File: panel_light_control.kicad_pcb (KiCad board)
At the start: 4 copper layers, 90 x 100 mm, 132 parts, among them J1 Conn_01x02, J11 RJ45_Shielded, J13 HR911105A, J2 RJ45_Shielded, J6 Conn_01x04, Q1 IRF540N, Q2 IRF540N, Q3 IRF540N, U1 L7805, U2 LM324, U3 STM32F207VGT6, U4 MCP2562-E-P, U5 LAN8720A, Y1 Crystal_GND24

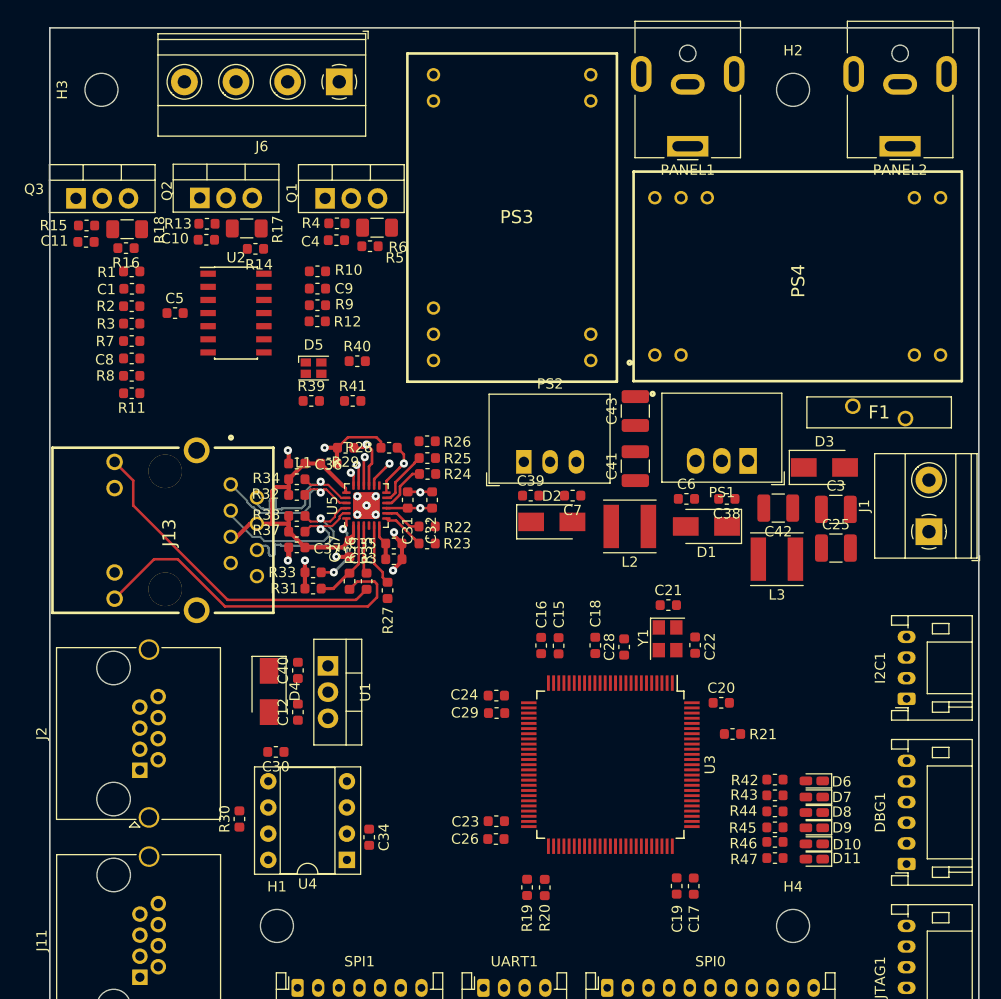
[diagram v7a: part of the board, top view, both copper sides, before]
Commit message: THT pad restring sizes increase for mechanical stability; generalized LED arrangement for more flexibility (8 bit display, CAN LED, PWM and general purpose RGB) and development-style look and feel; protection diode footprint is now THT to reduce reworking hassle should it short out due to misuse
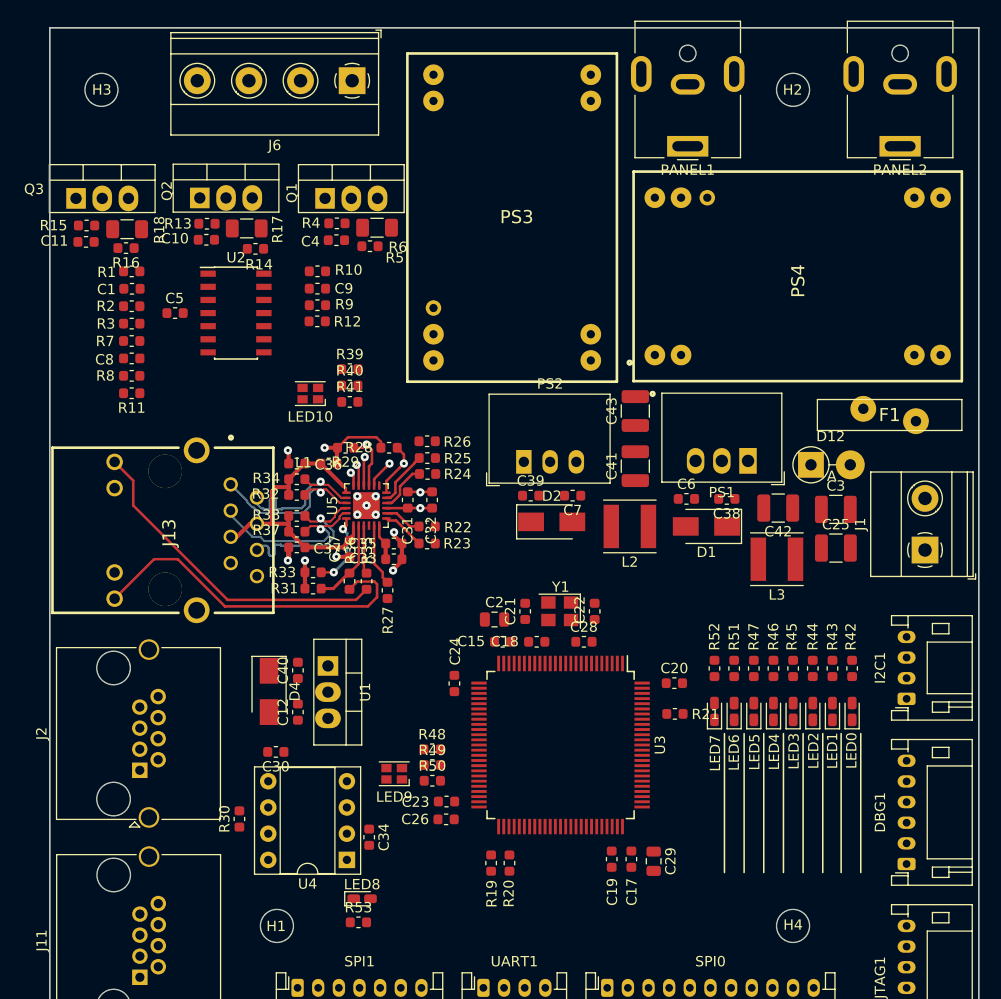
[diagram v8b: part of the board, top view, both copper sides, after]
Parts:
- removed C16: 100nF, Capacitor_SMD:C_0603_1608Metric
- removed D10: LED_WarmWhite, LED_SMD:LED_0603_1608Metric_Castellated
- removed D11: LED_ColdWhite, LED_SMD:LED_0603_1608Metric_Castellated
- removed D3: 1D4004, Diode_SMD:D_SMA
- removed D7: LED_R, LED_SMD:LED_0603_1608Metric_Castellated
- removed D8: LED_G, LED_SMD:LED_0603_1608Metric_Castellated
- removed D9: LED_B, LED_SMD:LED_0603_1608Metric_Castellated
- added C2: 4.7uF, Capacitor_SMD:C_0805_2012Metric, F.Cu at (143.1, 107.3)
- added D12: 1N4001, Diode_THT:D_DO-41_SOD81_P3.81mm_Vertical_AnodeUp, F.Cu at (173.7, 92.3)
- added LED1: LED_GN, LED_SMD:LED_0603_1608Metric_Castellated, F.Cu at (175.8, 116.2)
- added LED2: LED_GN, LED_SMD:LED_0603_1608Metric_Castellated, F.Cu at (173.9, 116.2)
- added LED3: LED_GN, LED_SMD:LED_0603_1608Metric_Castellated, F.Cu at (172.0, 116.2)
- added LED4: LED_GN, LED_SMD:LED_0603_1608Metric_Castellated, F.Cu at (170.1, 116.2)
- added LED5: LED_GN, LED_SMD:LED_0603_1608Metric_Castellated, F.Cu at (168.2, 116.2)
- added LED6: LED_GN, LED_SMD:LED_0603_1608Metric_Castellated, F.Cu at (166.3, 116.2)
- added LED7: LED_GN, LED_SMD:LED_0603_1608Metric_Castellated, F.Cu at (164.4, 116.2)
- added LED8: LED_GN, LED_SMD:LED_0603_1608Metric_Castellated, F.Cu at (130.3, 134.4)
- added LED9: RGB-PLCC4, LED_SMD:LED_Cree-PLCC4_2x2mm_CW, F.Cu at (133.4, 122.3)
- added R48: 220R, Resistor_SMD:R_0603_1608Metric, F.Cu at (137.0, 119.9)
- added R49: 1k, Resistor_SMD:R_0603_1608Metric, F.Cu at (137.1, 121.4)
- added R50: 1k, Resistor_SMD:R_0603_1608Metric, F.Cu at (137.1, 122.9)
- added R51: 120R, Resistor_SMD:R_0603_1608Metric, F.Cu at (166.3, 112.1)
- added R52: 120R, Resistor_SMD:R_0603_1608Metric, F.Cu at (164.4, 112.1)
- added R53: 120R, Resistor_SMD:R_0603_1608Metric, F.Cu at (129.9, 136.7)
- C29: footprint Capacitor_SMD:C_0603_1608Metric -> Capacitor_SMD:C_0805_2012Metric
- LED0: renamed from D6; value LED_CAN -> LED_GN
- LED10: renamed from D5; value LED_SYSTEM -> RGB-PLCC4
- moved C29 20.9 mm to (158.5, 130.7), turned to 270 degrees
- moved R47 18.5 mm to (168.2, 112.1), turned to 90 degrees
- moved R46 16.8 mm to (170.1, 112.1), turned to 90 degrees
- moved R45 15.5 mm to (172.0, 112.1), turned to 90 degrees
- moved R44 14.3 mm to (173.9, 112.1), turned to 90 degrees
- moved C21 13.9 mm to (146.1, 106.5), turned to 90 degrees
- moved R43 13.5 mm to (175.8, 112.1), turned to 90 degrees
- moved R42 13.1 mm to (177.7, 112.1), turned to 90 degrees
- moved Y1 10.8 mm to (149.4, 106.5), turned to 180 degrees
- moved C22 10.3 mm to (152.8, 106.5), turned to 270 degrees
- moved LED0 7.66 mm to (177.7, 116.2), turned to 90 degrees
- moved C19 6.81 mm to (154.4, 130.5)
- moved C17 6.58 mm to (156.3, 130.5)
- moved R21 5.91 mm to (160.6, 116.5)
- moved C18 5.69 mm to (147.2, 109.5), turned to 180 degrees
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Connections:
- R42 pad 2: LED_CAN -> LED0
- R43 pad 2: LED_R -> LED1
- R44 pad 2: LED_G -> LED2
- R45 pad 2: LED_B -> LED3
- R46 pad 2: LED_WW -> LED4
- R47 pad 2: LED_CW -> LED5
- U3 pad 1: Net-(U3-Pad1) -> LED2
- U3 pad 2: Net-(U3-Pad2) -> LED3
- U3 pad 3: LED_CW -> LED4
- U3 pad 38: LED_G -> LED7
- U3 pad 39: LED_R -> Net-(U3-Pad39)
- U3 pad 4: LED_WW -> LED5
- U3 pad 40: LED_CAN -> Net-(U3-Pad40)
- U3 pad 46: Net-(U3-Pad46) -> LED_CAN
- U3 pad 5: LED_B -> LED6
- U3 pad 97: Net-(U3-Pad97) -> LED0
- U3 pad 98: Net-(U3-Pad98) -> LED1
- Y1 pad 1: Net-(C21-Pad1) -> Net-(C22-Pad1)
- Y1 pad 3: Net-(C22-Pad1) -> Net-(C21-Pad1)
